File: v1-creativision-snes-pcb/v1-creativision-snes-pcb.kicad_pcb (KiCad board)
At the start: 2 copper layers, 66 x 71.6 mm, 14 parts, among them J1 Left Joystick, J2 Right Joystick, J4 PS/2 Keyboard, J5 SNES, J6 Debug, SW1 Reset Pico, U1 Pico, U2 TRANSCEIVER-8BIT, U3 TRANSCEIVER-8BIT

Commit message: Add diode to prevent backpowering when uploading firmware
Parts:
- added D1: D, Diode_THT:D_DO-15_P10.16mm_Horizontal, F.Cu at (97.2, 40.6)
- U2, U3: value TRANSCEIVER-8BIT -> LOGIC-SN74LVC245AN(DIP20-7.62MM)
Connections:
- U1 pad 39: +5V -> Net-(D1-K)
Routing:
- net Net-(D1-K): track 0.00 -> 83.9 mm, vias 0 -> 2
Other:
- board text added: "CreatiVision V1 controller bodge board 2023-25 leadedsolder.com v0.2"
- board text removed: "CreatiVision V1 controller bodge board 2023 leadedsolder.com v0.1"

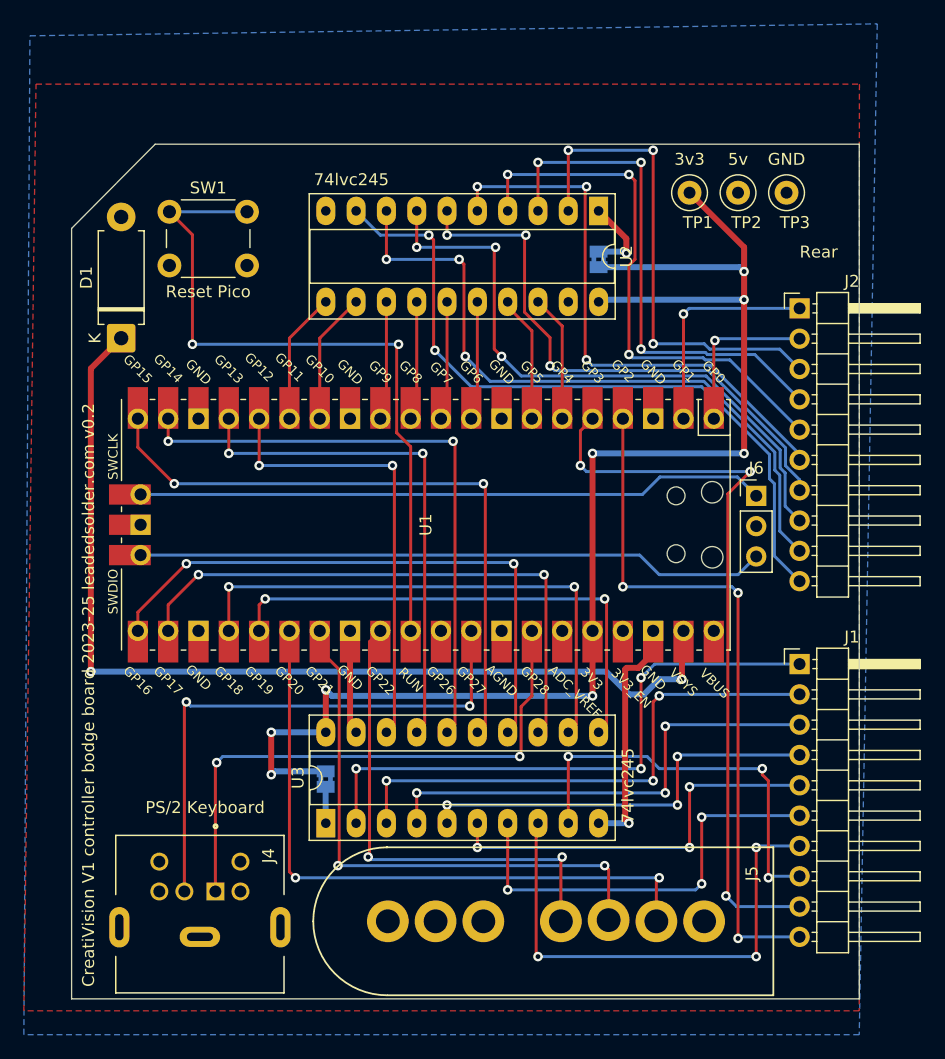
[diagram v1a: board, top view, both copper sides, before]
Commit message: Fix DIR pin error
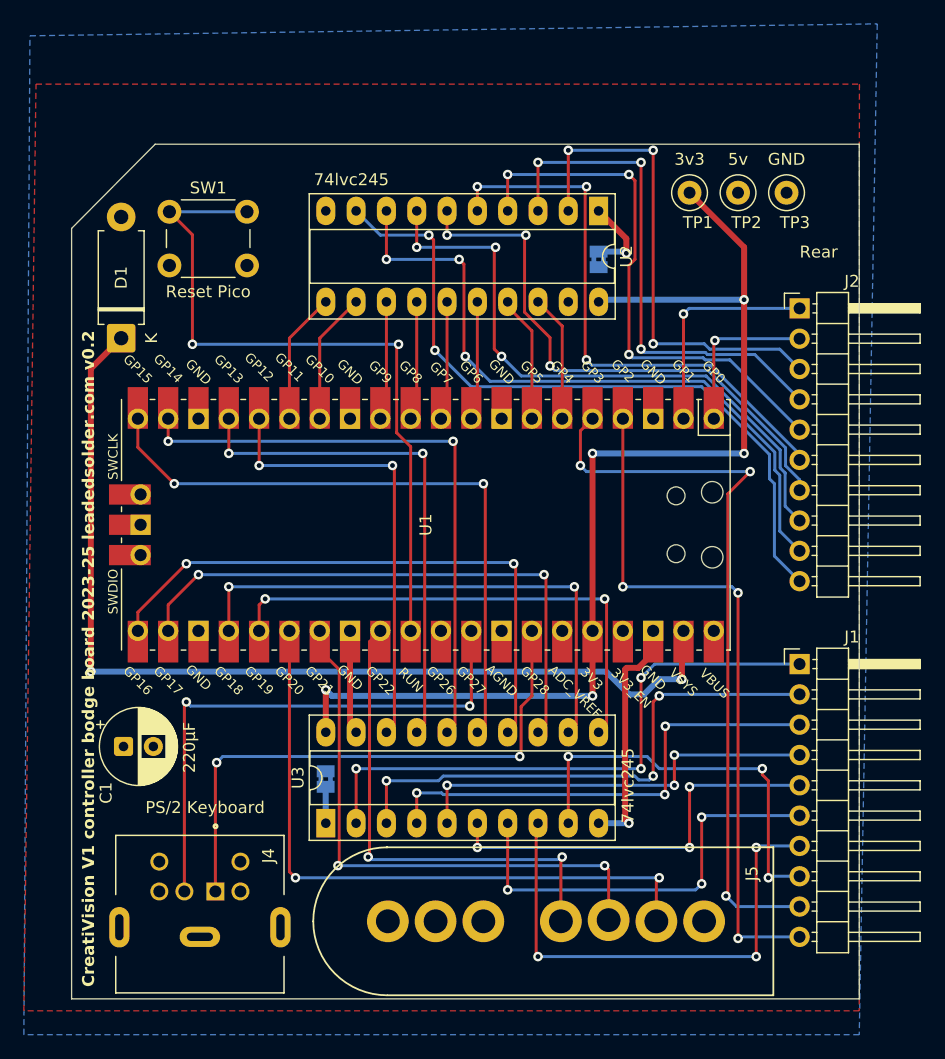
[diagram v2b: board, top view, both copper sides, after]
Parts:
- removed J6: Debug, Connector_PinHeader_2.54mm:PinHeader_1x03_P2.54mm_Vertical
- added C1: 220µF, Capacitor_THT:CP_Radial_D6.3mm_P2.50mm, F.Cu at (97.3, 74.8)
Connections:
- JP1 pad 2: +3.3V -> GND
- JP2 pad 2: +3.3V -> GND
- U1 pad 41: /SWCLK -> unconnected-(U1-SWCLK-Pad41)_1
- U1 pad 42: GND -> unconnected-(U1-GND-Pad42)_1
- U1 pad 43: /SWDIO -> unconnected-(U1-SWDIO-Pad43)
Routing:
- net /SWDIO: track 52.9 -> 0.00 mm
- net /SWCLK: track 52.8 -> 0.00 mm
- net +3.3V: track 120.3 -> 95.1 mm, vias 8 -> 5
